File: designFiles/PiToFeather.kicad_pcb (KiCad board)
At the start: 2 copper layers, 65 x 56 mm, 9 parts, among them U1 piHeader, U2 featherHeader_12pin, U3 featherHeader_16pin, U4 featherHeader_12pin, U5 featherHeader_16pin

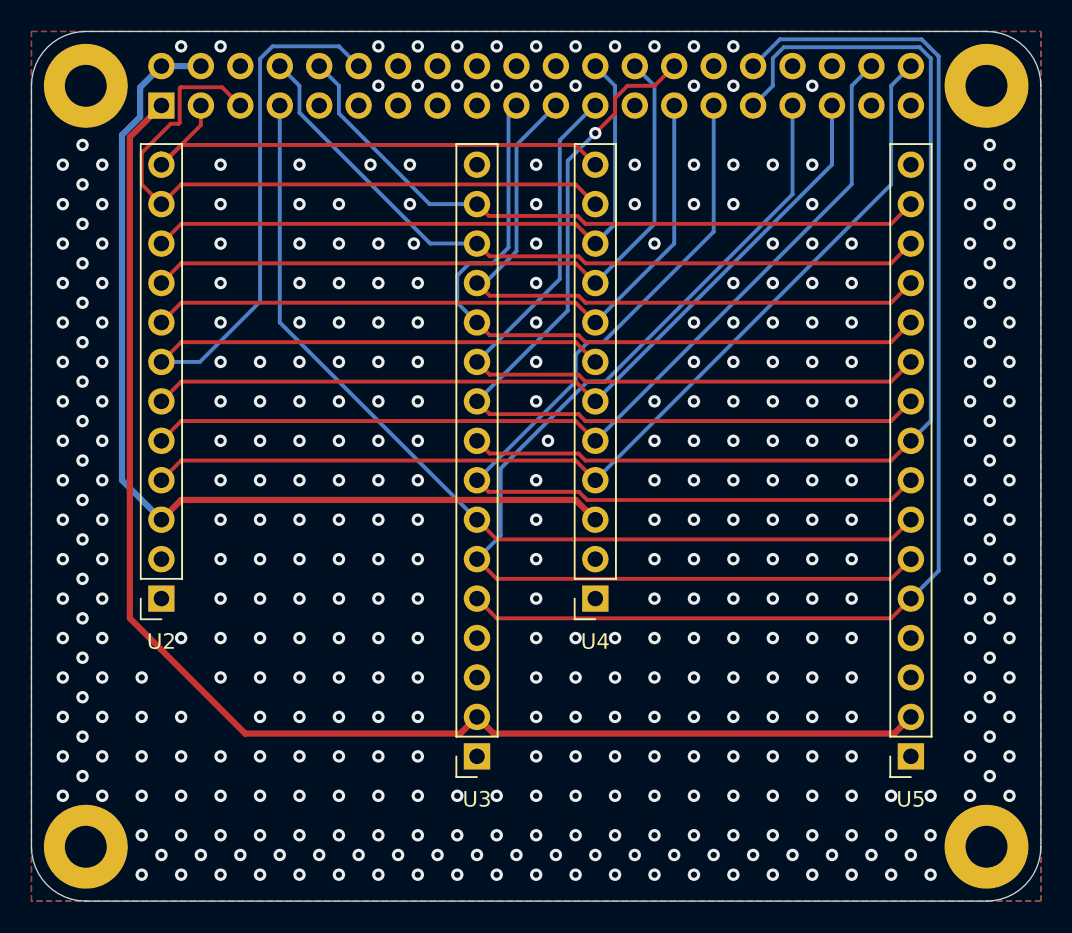
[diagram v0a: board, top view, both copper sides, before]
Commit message: Change of RX and TX
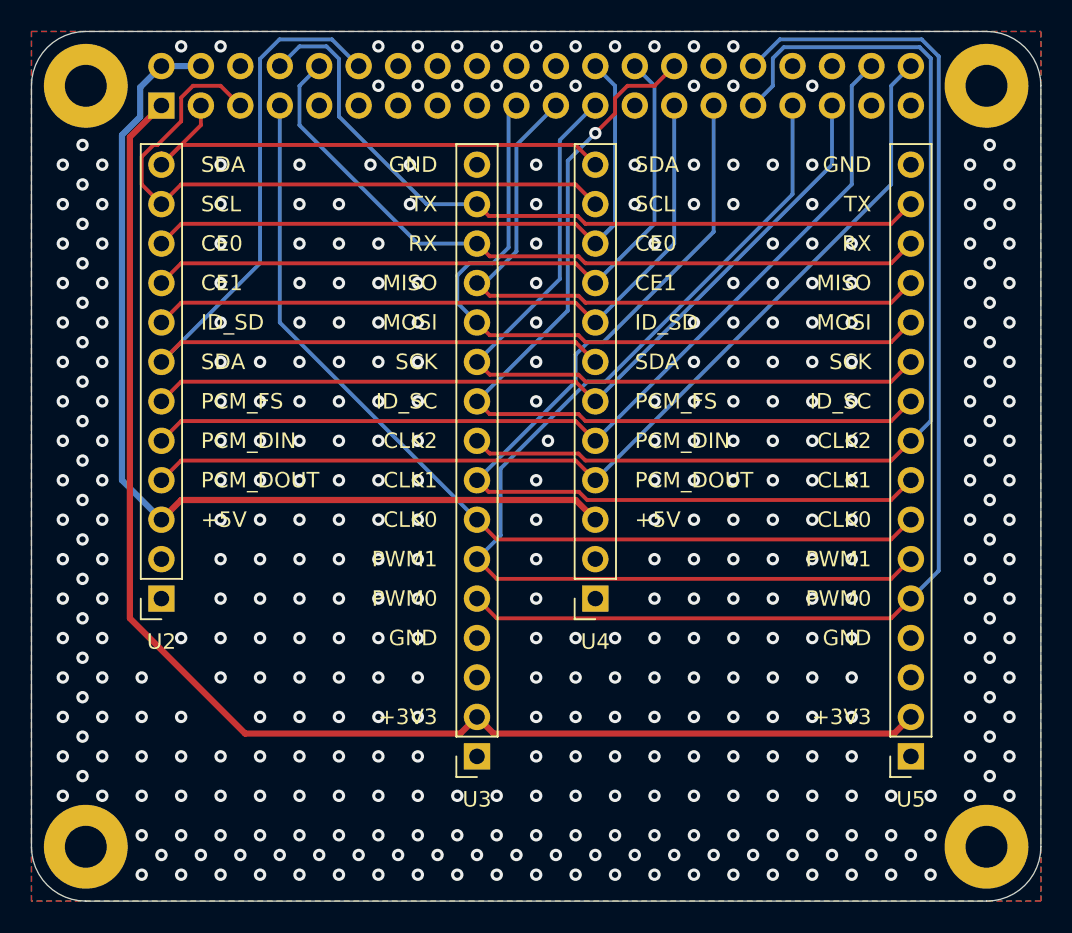
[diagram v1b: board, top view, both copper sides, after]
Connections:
- U3 pad 14: TX -> RX
- U3 pad 15: RX -> TX
- U5 pad 14: TX -> RX
- U5 pad 15: RX -> TX
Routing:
- net RX: track 43.9 -> 47.9 mm
- net TX: track 47.4 -> 48.6 mm
- net PCM_CLK: track 59.8 -> 58.7 mm
- net GND: vias 411 -> 410
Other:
- board text added: "+3V3"
- board text added: "+5V"
- board text added: "CE0"
- board text added: "CE1"
- board text added: "CLK0"
- board text added: "CLK1"
- board text added: "CLK2"
- board text added: "GND"
- board text added: "ID_SC"
- board text added: "ID_SD"
- board text added: "MISO"
- board text added: "MOSI"
- board text added: "PCM_DIN"
- board text added: "PCM_DOUT"
- board text added: "PCM_FS"
- board text added: "PWM0"
- board text added: "PWM1"
- board text added: "RX"
- board text added: "SCK"
- board text added: "SCL"
- board text added: "SDA"
- board text added: "TX"
